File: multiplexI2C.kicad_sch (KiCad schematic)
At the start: 15 parts, among them U1 PCA9548A

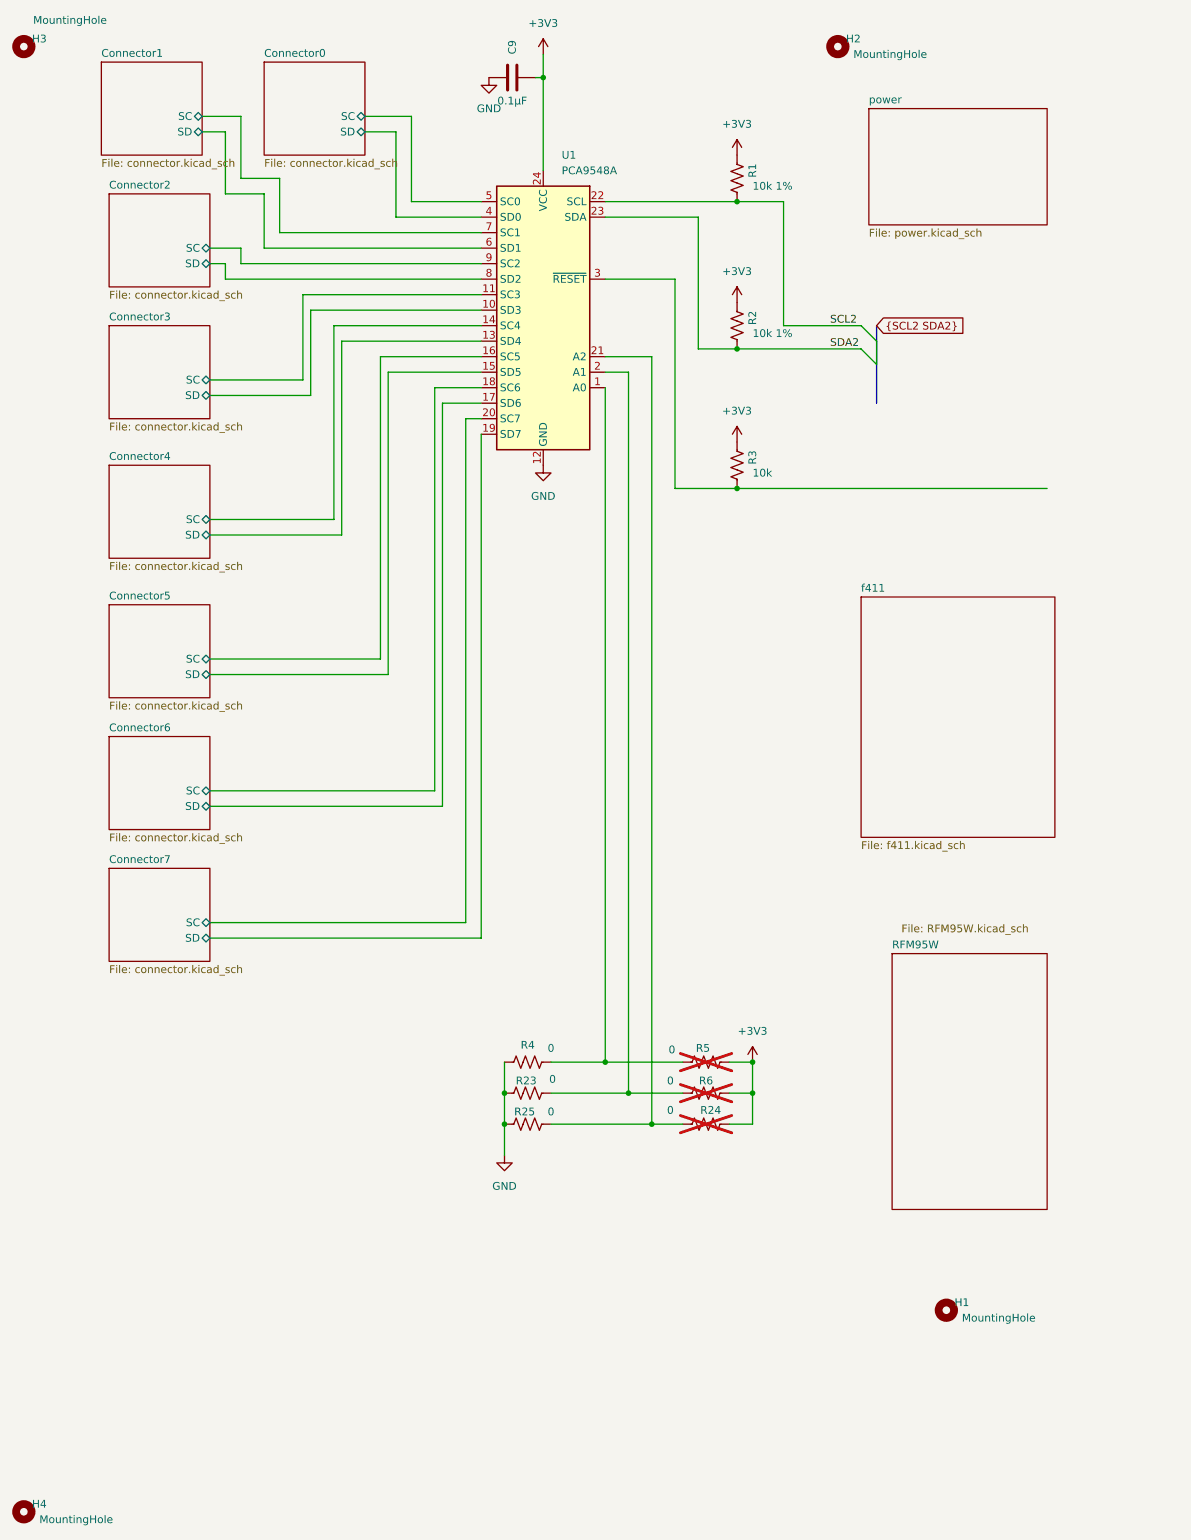
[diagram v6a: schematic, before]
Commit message: symbols an footprints added for f411 change. ERC passes.
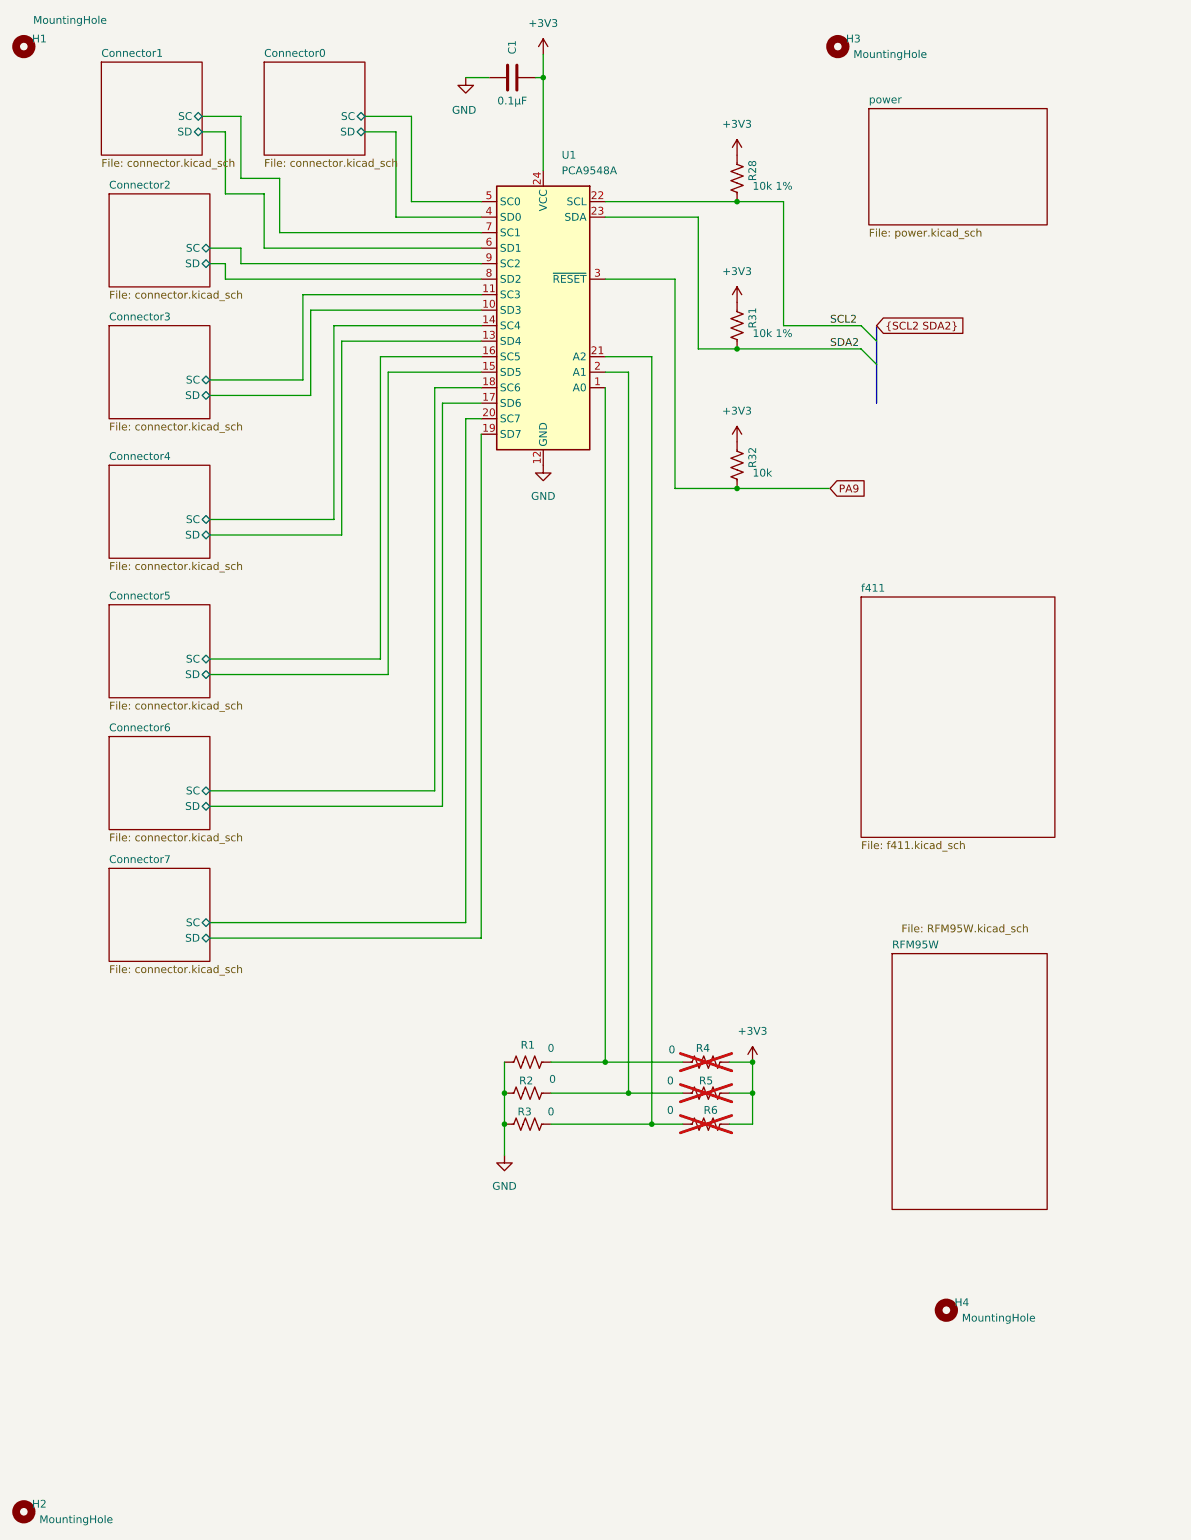
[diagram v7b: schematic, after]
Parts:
- U1: footprint ProjectLib:TSSOP-24_4.4x7.8mm_P0.65mm -> Package_SO:TSSOP-24_4.4x7.8mm_P0.65mm
- renumbered C9 to C1, H3 to H1, H4 to H2, H2 to H3, H1 to H4, R4 to R1, R23 to R2, R1 to R28, R25 to R3, R2 to R31, R3 to R32, R5 to R4, R6 to R5, R24 to R6
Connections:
- net PA9: now reaches R32.2, U1.3 (~{RESET})
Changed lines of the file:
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@@
+	)
+	(junction
+		(at 135.89 92.71)
+		(diameter 0)
+		(color 0 0 0 0)
 	)
 	(junction
@@
 	)
 	(junction
-		(at 135.89 92.71)
-		(diameter 0)
-		(color 0 0 0 0)
-	)
-	(junction
 		(at 104.14 25.4)
 		(diameter 0)
@@
 	(wire
 		(pts
+			(xy 91.44 25.4) (xy 95.25 25.4)
+		)
+		(stroke
+			(width 0)
+			(type default)
+		)
+	)
+	(wire
+		(pts
 			(xy 49.53 55.88) (xy 52.07 55.88)
 		)
@@
 	(wire
 		(pts
+			(xy 135.89 92.71) (xy 151.13 92.71)
+		)
+		(stroke
+			(width 0)
+			(type default)
+		)
+	)
+	(wire
+		(pts
 			(xy 52.07 55.88) (xy 52.07 58.42)
 		)
@@
 	(wire
 		(pts
-			(xy 158.75 68.58) (xy 158.75 72.39)
-		)
-		(stroke
-			(width 0)
-			(type default)
-		)
-	)
-	(wire
-		(pts
 			(xy 49.53 100.33) (xy 71.12 100.33)
 		)
@@
 		(pts
 			(xy 105.41 191.77) (xy 118.11 191.77)
-		)
-		(stroke
-			(width 0)
-			(type default)
-		)
-	)
-	(wire
-		(pts
-			(xy 135.89 92.71) (xy 186.69 92.71)
 		)
 		(stroke
@@
 			)
 			(justify left bottom)
+		)
+	)
+	(global_label "PA9"
+		(shape input)
+		(at 151.13 92.71 0)
+		(fields_autoplaced yes)
+		(effects
+			(font
+				(size 1.27 1.27)
+			)
+			(justify left)
+		)
+		(property "Intersheetrefs" "${INTERSHEET_REFS}"
+			(at 157.6833 92.71 0)
+			(effects
+				(font
+					(size 1.27 1.27)
+				)
+				(justify left)
+				(hide yes)
+			)
 		)
 	)
@@
 		(on_board yes)
 		(dnp no)
-		(property "Reference" "C9"
+		(property "Reference" "C1"
 			(at 99.06 21.59 0)
 			(effects
@@
 			(project "multiplexI2CwithRJ11"
 				(path "/0c2d0c14-8850-4a30-bb78-b2f40cb442ba"
-					(reference "C9")
+					(reference "C1")
 					(unit 1)
 				)
@@
 		(on_board yes)
 		(dnp no)
-		(property "Reference" "R23"
+		(property "Reference" "R2"
 			(at 101.346 189.738 90)
 			(effects
@@
 			(project "multiplexI2CwithRJ11"
 				(path "/0c2d0c14-8850-4a30-bb78-b2f40cb442ba"
-					(reference "R23")
+					(reference "R2")
 					(unit 1)
 				)
@@
 		(dnp no)
 		(fields_autoplaced yes)
-		(property "Reference" "#PWR031"
+		(property "Reference" "#PWR07"
 			(at 135.89 66.04 0)
 			(effects
@@
 			(project "multiplexI2CwithRJ11"
 				(path "/0c2d0c14-8850-4a30-bb78-b2f40cb442ba"
-					(reference "#PWR031")
+					(reference "#PWR07")
 					(unit 1)
 				)
@@
 		(dnp no)
 		(fields_autoplaced yes)
-		(property "Reference" "#PWR029"
+		(property "Reference" "#PWR04"
 			(at 104.14 25.4 0)
 			(effects
@@
 			(project "multiplexI2CwithRJ11"
 				(path "/0c2d0c14-8850-4a30-bb78-b2f40cb442ba"
-					(reference "#PWR029")
+					(reference "#PWR04")
 					(unit 1)
 				)
@@
 		(dnp no)
 		(fields_autoplaced yes)
-		(property "Reference" "#PWR012"
+		(property "Reference" "#PWR05"
 			(at 104.14 95.25 0)
 			(effects
@@
 			(project "multiplexI2CwithRJ11"
 				(path "/0c2d0c14-8850-4a30-bb78-b2f40cb442ba"
-					(reference "#PWR012")
+					(reference "#PWR05")
 					(unit 1)
 				)
@@
 		(dnp no)
 		(fields_autoplaced yes)
-		(property "Reference" "#PWR01"
+		(property "Reference" "#PWR09"
 			(at 138.43 190.5 0)
 			(effects
@@
 			(project ""
 				(path "/0c2d0c14-8850-4a30-bb78-b2f40cb442ba"
-					(reference "#PWR01")
+					(reference "#PWR09")
 					(unit 1)
 				)
@@
 		(on_board yes)
 		(dnp no)
-		(property "Reference" "H3"
+		(property "Reference" "H1"
 			(at 21.59 19.05 0)
 			(effects
@@
 			(project "multiplexI2CwithRJ11"
 				(path "/0c2d0c14-8850-4a30-bb78-b2f40cb442ba"
-					(reference "H3")
+					(reference "H1")
 					(unit 1)
 				)
@@
 		(on_board yes)
 		(dnp no)
-		(property "Reference" "R25"
+		(property "Reference" "R3"
 			(at 101.092 194.818 90)
 			(effects
@@
 			(project "multiplexI2CwithRJ11"
 				(path "/0c2d0c14-8850-4a30-bb78-b2f40cb442ba"
-					(reference "R25")
+					(reference "R3")
 					(unit 1)
 				)
@@
 		(on_board yes)
 		(dnp yes)
-		(property "Reference" "R5"
+		(property "Reference" "R4"
 			(at 130.302 184.404 90)
 			(effects
@@
 			(project "multiplexI2C"
 				(path "/0c2d0c14-8850-4a30-bb78-b2f40cb442ba"
-					(reference "R5")
+					(reference "R4")
 					(unit 1)
 				)
@@
 		(dnp no)
 		(fields_autoplaced yes)
-		(property "Reference" "H4"
+		(property "Reference" "H2"
 			(at 21.59 259.08 0)
 			(effects
@@
 			(project "multiplexI2CwithRJ11"
 				(path "/0c2d0c14-8850-4a30-bb78-b2f40cb442ba"
-					(reference "H4")
+					(reference "H2")
 					(unit 1)
 				)
@@
 		(on_board yes)
 		(dnp no)
-		(property "Reference" "R4"
+		(property "Reference" "R1"
 			(at 101.6 183.896 90)
 			(effects
@@
 			(project "multiplexI2CwithRJ11"
 				(path "/0c2d0c14-8850-4a30-bb78-b2f40cb442ba"
-					(reference "R4")
+					(reference "R1")
 					(unit 1)
 				)
@@
 		(dnp no)
 		(fields_autoplaced yes)
-		(property "Reference" "R2"
+		(property "Reference" "R31"
 			(at 138.43 64.77 90)
 			(effects
@@
 			(project "multiplexI2CwithRJ11"
 				(path "/0c2d0c14-8850-4a30-bb78-b2f40cb442ba"
-					(reference "R2")
+					(reference "R31")
 					(unit 1)
 				)
@@
 	(symbol
 		(lib_id "power:GND")
-		(at 95.25 25.4 0)
+		(at 91.44 25.4 0)
 		(mirror y)
 		(unit 1)
@@
 		(on_board yes)
 		(dnp no)
-		(fields_autoplaced yes)
-		(property "Reference" "#PWR019"
-			(at 95.25 31.75 0)
+		(property "Reference" "#PWR01"
+			(at 91.44 31.75 0)
 			(effects
 				(font
@@
 		)
 		(property "Value" "GND"
-			(at 95.25 30.48 0)
+			(at 91.186 30.734 0)
 			(effects
 				(font
@@
 		)
 		(property "Footprint" ""
-			(at 95.25 25.4 0)
+			(at 91.44 25.4 0)
 			(effects
 				(font
@@
 		)
 		(property "Datasheet" ""
-			(at 95.25 25.4 0)
+			(at 91.44 25.4 0)
 			(effects
 				(font
@@
 		)
 		(property "Description" "Power symbol creates a global label with name \"GND\" , ground"
-			(at 95.25 25.4 0)
+			(at 91.44 25.4 0)
 			(effects
 				(font
@@
 			(project "multiplexI2CwithRJ11"
 				(path "/0c2d0c14-8850-4a30-bb78-b2f40cb442ba"
-					(reference "#PWR019")
+					(reference "#PWR01")
 					(unit 1)
 				)
@@
 		(dnp no)
 		(fields_autoplaced yes)
-		(property "Reference" "H1"
+		(property "Reference" "H4"
 			(at 172.72 226.06 0)
 			(effects
@@
 			(project "multiplexI2CwithRJ11"
 				(path "/0c2d0c14-8850-4a30-bb78-b2f40cb442ba"
-					(reference "H1")
+					(reference "H4")
 					(unit 1)
 				)
@@
 		(dnp no)
 		(fields_autoplaced yes)
-		(property "Reference" "H2"
+		(property "Reference" "H3"
 			(at 154.94 19.05 0)
 			(effects
@@
 			(project "multiplexI2CwithRJ11"
 				(path "/0c2d0c14-8850-4a30-bb78-b2f40cb442ba"
-					(reference "H2")
+					(reference "H3")
 					(unit 1)
 				)
@@
 		(dnp no)
 		(fields_autoplaced yes)
-		(property "Reference" "R1"
+		(property "Reference" "R28"
 			(at 138.43 40.64 90)
 			(effects
@@
 			(project "multiplexI2CwithRJ11"
 				(path "/0c2d0c14-8850-4a30-bb78-b2f40cb442ba"
-					(reference "R1")
+					(reference "R28")
 					(unit 1)
 				)
@@
 			)
 		)
-		(property "Footprint" "ProjectLib:TSSOP-24_4.4x7.8mm_P0.65mm"
+		(property "Footprint" "Package_SO:TSSOP-24_4.4x7.8mm_P0.65mm"
 			(at 104.14 88.9 0)
 			(effects
@@
 			)
 		)
-		(property "Datasheet" "https://www.nxp.com/products/interfaces/ic-spi-i3c-interface-devices/ic-logic-multiplexers-switches/eight-channel-ic-bus-switch-with-reset:PCA9548A"
+		(property "Datasheet" "http://www.ti.com/lit/ds/symlink/tca9548a.pdf"
 			(at 102.87 57.15 0)
 			(effects
@@
 		(dnp no)
 		(fields_autoplaced yes)
-		(property "Reference" "#PWR032"
+		(property "Reference" "#PWR08"
 			(at 135.89 88.9 0)
 			(effects
@@
 			(project "multiplexI2CwithRJ11"
 				(path "/0c2d0c14-8850-4a30-bb78-b2f40cb442ba"
-					(reference "#PWR032")
+					(reference "#PWR08")
 					(unit 1)
 				)
@@
 		(on_board yes)
 		(dnp yes)
-		(property "Reference" "R6"
+		(property "Reference" "R5"
 			(at 130.81 189.738 90)
 			(effects
@@
 			(project "multiplexI2C"
 				(path "/0c2d0c14-8850-4a30-bb78-b2f40cb442ba"
-					(reference "R6")
+					(reference "R5")
 					(unit 1)
 				)
@@
 		(dnp no)
 		(fields_autoplaced yes)
-		(property "Reference" "#PWR030"
+		(property "Reference" "#PWR06"
 			(at 135.89 41.91 0)
 			(effects
@@
 			(project "multiplexI2CwithRJ11"
 				(path "/0c2d0c14-8850-4a30-bb78-b2f40cb442ba"
-					(reference "#PWR030")
+					(reference "#PWR06")
 					(unit 1)
 				)
@@
 		(on_board yes)
 		(dnp yes)
-		(property "Reference" "R24"
+		(property "Reference" "R6"
 			(at 131.572 194.564 90)
 			(effects
@@
 			(project "multiplexI2C"
 				(path "/0c2d0c14-8850-4a30-bb78-b2f40cb442ba"
-					(reference "R24")
+					(reference "R6")
 					(unit 1)
 				)
@@
 		(dnp no)
 		(fields_autoplaced yes)
-		(property "Reference" "R3"
+		(property "Reference" "R32"
 			(at 138.43 87.63 90)
 			(effects
@@
 			(project "multiplexI2CwithRJ11"
 				(path "/0c2d0c14-8850-4a30-bb78-b2f40cb442ba"
-					(reference "R3")
+					(reference "R32")
 					(unit 1)
 				)

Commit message: ongoing
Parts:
- C1: footprint ProjectLib:C_0805_2012Metric -> ProjectLib:C_0402_1005Metric
- R1, R2, R28, R3, R31, R32, R4, R5, R6: footprint ProjectLib:R_0603_1608Metric -> ProjectLib:R_0402_1005Metric
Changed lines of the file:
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@@
 			)
 		)
-		(property "Footprint" "ProjectLib:C_0805_2012Metric"
+		(property "Footprint" "ProjectLib:C_0402_1005Metric"
 			(at 95.25 24.4348 0)
 			(effects
@@
 			)
 		)
-		(property "Footprint" "ProjectLib:R_0603_1608Metric"
+		(property "Footprint" "ProjectLib:R_0402_1005Metric"
 			(at 101.346 192.786 90)
 			(effects
@@
 			)
 		)
-		(property "Footprint" "ProjectLib:R_0603_1608Metric"
+		(property "Footprint" "ProjectLib:R_0402_1005Metric"
 			(at 101.346 197.866 90)
 			(effects
@@
 			)
 		)
-		(property "Footprint" "ProjectLib:R_0603_1608Metric"
+		(property "Footprint" "ProjectLib:R_0402_1005Metric"
 			(at 130.556 187.706 90)
 			(effects
@@
 			)
 		)
-		(property "Footprint" "ProjectLib:R_0603_1608Metric"
+		(property "Footprint" "ProjectLib:R_0402_1005Metric"
 			(at 101.346 187.706 90)
 			(effects
@@
 			)
 		)
-		(property "Footprint" "ProjectLib:R_0603_1608Metric"
+		(property "Footprint" "ProjectLib:R_0402_1005Metric"
 			(at 136.906 66.294 90)
 			(effects
@@
 			)
 		)
-		(property "Footprint" "ProjectLib:R_0603_1608Metric"
+		(property "Footprint" "ProjectLib:R_0402_1005Metric"
 			(at 136.906 42.164 90)
 			(effects
@@
 			)
 		)
-		(property "Footprint" "ProjectLib:R_0603_1608Metric"
+		(property "Footprint" "ProjectLib:R_0402_1005Metric"
 			(at 130.556 192.786 90)
 			(effects
@@
 			)
 		)
-		(property "Footprint" "ProjectLib:R_0603_1608Metric"
+		(property "Footprint" "ProjectLib:R_0402_1005Metric"
 			(at 130.556 197.866 90)
 			(effects
@@
 			)
 		)
-		(property "Footprint" "ProjectLib:R_0603_1608Metric"
+		(property "Footprint" "ProjectLib:R_0402_1005Metric"
 			(at 136.906 89.154 90)
 			(effects
